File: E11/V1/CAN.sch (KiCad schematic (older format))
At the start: 21 parts, among them J401 649006227222, J402 649006227222, U401 SN65HVD232DR

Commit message: update for missing resistor
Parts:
- removed J401, J402: 649006227222, Connectors:649006227222, symbol Connectors:649006227222
- added J401, J402: 64900621122, Connectors:64900621122, symbol Connectors:64900621122
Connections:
- wire segments 67 -> 87
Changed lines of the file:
@@
 EESchema Schematic File Version 4
+LIBS:Slave-cache
 EELAYER 30 0
 EELAYER END
@@
 	2900 3800 3100 3800
 Wire Wire Line
-	1700 4000 3100 4000
+	1700 4000 1800 4000
 Connection ~ 1800 4000
 Wire Wire Line
@@
 	2900 3400 2800 3400
 Wire Wire Line
-	2900 2900 2900 3800
+	2900 2900 2900 3000
 Connection ~ 2900 3400
 $Comp
@@
 	2500 3000 2400 3000
 Wire Wire Line
-	2400 3000 2400 3500
+	2400 3000 2400 3400
 Connection ~ 2400 3400
 $Comp
@@
 	6300 3200 6300 3300
 Wire Wire Line
-	5300 5100 6400 5100
-Wire Wire Line
-	5400 4900 6400 4900
+	5300 5100 5600 5100
+Wire Wire Line
+	5400 4900 6000 4900
 Wire Wire Line
 	5400 4000 5400 4900
 Wire Wire Line
-	3800 4000 5400 4000
-Wire Wire Line
-	3800 4200 5300 4200
+	3800 4000 4200 4000
+Wire Wire Line
+	3800 4200 4200 4200
 Wire Wire Line
 	5300 4200 5300 5100
 Wire Wire Line
-	5100 2500 6500 2500
+	5100 2500 5700 2500
 Wire Wire Line
 	5700 2500 5700 2900
 Wire Wire Line
-	5200 2700 6500 2700
+	5200 2700 6200 2700
 Wire Wire Line
 	6300 2700 6300 2900
@@
 Connection ~ 6200 2700
 $Comp
-L Connectors:649006227222 J401
-U 1 1 593E0605
-P 7100 1900
-F 0 "J401" H 7100 2200 60  0000 C CNN
-F 1 "649006227222" H 7100 1750 60  0000 C CNN
-F 2 "Connectors:649006227222" H 7100 1000 60  0001 C CNN
-F 3 "http://katalog.we-online.de/em/datasheet/649006227222.pdf" H 7100 900 60  0001 C CNN
-F 4 "Digikey" H 7100 1500 60  0001 C CNN "Supplier"
-F 5 "732-1939-ND" H 7100 1400 60  0001 C CNN "Supplier Part Number"
-F 6 "Wurth Electronics Inc." H 7100 1300 60  0001 C CNN "Manufacturer"
-F 7 "649006227222" H 7100 1200 60  0001 C CNN "Manufacturer Part Number"
-F 8 "HEADER MALE DUAL ANGLE W/MNT 6P" H 7100 1100 60  0001 C CNN "Description"
-	1    7100 1900
-	1    0    0    -1
-$EndComp
-$Comp
 L Resistors:RC0805JR-070RL R403
 U 1 1 593E067F
@@
 Text Label 6500 4300 0    60   ~ 0
 CAN_N
-$Comp
-L Connectors:649006227222 J402
-U 1 1 593E12E2
-P 7100 4300
-F 0 "J402" H 7100 4600 60  0000 C CNN
-F 1 "649006227222" H 7100 4150 60  0000 C CNN
-F 2 "Connectors:649006227222" H 7100 3400 60  0001 C CNN
-F 3 "http://katalog.we-online.de/em/datasheet/649006227222.pdf" H 7100 3300 60  0001 C CNN
-F 4 "Digikey" H 7100 3900 60  0001 C CNN "Supplier"
-F 5 "732-1939-ND" H 7100 3800 60  0001 C CNN "Supplier Part Number"
-F 6 "Wurth Electronics Inc." H 7100 3700 60  0001 C CNN "Manufacturer"
-F 7 "649006227222" H 7100 3600 60  0001 C CNN "Manufacturer Part Number"
-F 8 "HEADER MALE DUAL ANGLE W/MNT 6P" H 7100 3500 60  0001 C CNN "Description"
-	1    7100 4300
-	1    0    0    -1
-$EndComp
 $Comp
 L Resistors:RC0805JR-070RL R404
@@
 $EndComp
 Wire Wire Line
-	2300 4200 2600 4200
+	2300 4200 2500 4200
 Wire Wire Line
 	3000 4200 3100 4200
+Wire Wire Line
+	1800 4000 1900 4000
+Wire Wire Line
+	2900 3400 2900 3800
+Wire Wire Line
+	2900 3000 2900 3400
+Wire Wire Line
+	2400 3400 2400 3500
+Wire Wire Line
+	5200 4200 5300 4200
+Wire Wire Line
+	6300 2700 6500 2700
+Wire Wire Line
+	5700 2500 6300 2500
+Wire Wire Line
+	5100 4000 5400 4000
+Wire Wire Line
+	4400 4000 5100 4000
+Wire Wire Line
+	4800 4200 5200 4200
+Wire Wire Line
+	4200 4200 4800 4200
+Wire Wire Line
+	4200 4000 4400 4000
+Wire Wire Line
+	1900 4000 3100 4000
+Wire Wire Line
+	2500 4200 2600 4200
+Wire Wire Line
+	5600 5100 6100 5100
+Wire Wire Line
+	6100 5100 6400 5100
+Wire Wire Line
+	6200 4900 6400 4900
+Wire Wire Line
+	6300 2500 6500 2500
+Wire Wire Line
+	6200 2700 6300 2700
+Wire Wire Line
+	6000 4900 6200 4900
+$Comp
+L Connectors:64900621122 J401
+U 1 1 5EB2172E
+P 7100 1900
+F 0 "J401" H 7100 2337 60  0000 C CNN
+F 1 "64900621122" H 7100 2231 60  0000 C CNN
+F 2 "Connectors:64900621122" H 7100 1000 60  0001 C CNN
+F 3 "http://katalog.we-online.de/em/datasheet/6490xx21122.pdf" H 7100 900 60  0001 C CNN
+F 4 "Digikey" H 7100 1500 60  0001 C CNN "Supplier"
+F 5 "732-1929-ND" H 7100 1400 60  0001 C CNN "Supplier Part Number"
+F 6 "Wurth Electronics Inc." H 7100 1300 60  0001 C CNN "Manufacturer"
+F 7 "64900621122" H 7100 1200 60  0001 C CNN "Manufacturer Part Number"
+F 8 "HEADER MALE 4.20MM DUAL VERT 6P" H 7100 1100 60  0001 C CNN "Description"
+	1    7100 1900
+	1    0    0    -1
+$EndComp
+$Comp
+L Connectors:64900621122 J402
+U 1 1 5EB22637
+P 7100 4300
+F 0 "J402" H 7100 4737 60  0000 C CNN
+F 1 "64900621122" H 7100 4631 60  0000 C CNN
+F 2 "Connectors:64900621122" H 7100 3400 60  0001 C CNN
+F 3 "http://katalog.we-online.de/em/datasheet/6490xx21122.pdf" H 7100 3300 60  0001 C CNN
+F 4 "Digikey" H 7100 3900 60  0001 C CNN "Supplier"
+F 5 "732-1929-ND" H 7100 3800 60  0001 C CNN "Supplier Part Number"
+F 6 "Wurth Electronics Inc." H 7100 3700 60  0001 C CNN "Manufacturer"
+F 7 "64900621122" H 7100 3600 60  0001 C CNN "Manufacturer Part Number"
+F 8 "HEADER MALE 4.20MM DUAL VERT 6P" H 7100 3500 60  0001 C CNN "Description"
+	1    7100 4300
+	1    0    0    -1
+$EndComp
 $EndSCHEMATC

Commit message: most of the parts have been migrated to new board outline
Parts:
- C401: footprint Capacitors:C0805 -> Capacitors:C0603; symbol Capacitors:885012107015 -> Capacitors:885012106022; Description CAP CER 1UF 25V X5R 0805 -> CAP CER 1UF 25V X5R 0603; Manufacturer Part Number 885012107015 -> 885012106022; Supplier Part Number 732-7625-1-ND -> 732-7919-2-ND
- C402, C403, C406, C407: footprint Capacitors:C0805 -> Capacitors:C0603; symbol Capacitors:885012007053 -> Capacitors:885012006053; Description CAP CER 22PF 50V C0G/NP0 0805 -> CAP CER 22PF 50V X7R 0603; Manufacturer Part Number 885012007053 -> 885012206077; Supplier Part Number 732-7848-1-ND -> 732-7995-2-ND
- C404: footprint Capacitors:C0805 -> Capacitors:C0603; symbol Capacitors:885012207098 -> Capacitors:885012206095; Description CAP CER 0.1UF 50V X7R 0805 -> CAP CER 0.1UF 50V X7R 0603; Manufacturer Part Number 885012207098 -> 885012206095; Supplier Part Number 732-8080-1-ND -> 732-8013-2-ND
- C405: footprint Capacitors:C0805 -> Capacitors:C0603; symbol Capacitors:885012207080 -> Capacitors:885012206077; Description CAP CER 100PF 50V X7R 0805 -> CAP CER 100PF 50V X7R 0603; Manufacturer Part Number 885012207080 -> 885012206077; Supplier Part Number 732-8062-1-ND -> 732-7995-2-ND
- R401, R405: footprint Resistors:R0805 -> Resistors:R0603; symbol Resistors:RC0805JR-07100RL -> Resistors:RNCP0603FTD100R; Description RES SMD 100 OHM 5% 1/8W 0805 -> RES 100 OHM 1% 1/8W 0603; Manufacturer Yageo -> Stackpole Electronics Inc; Manufacturer Part Number RC0805JR-07100RL -> RNCP0603FTD100R; Supplier Part Number 311-100ARCT-ND -> RNCP0603FTD100RTR-ND
- R403, R404: footprint Resistors:R0805 -> Resistors:R0603; symbol Resistors:RC0805JR-070RL -> Resistors:RC0603JR-070RL; Description RES SMD 0.0 OHM JUMPER 1/8W 0805 -> RES SMD 0 OHM JUMPER 1/10W 0603; Manufacturer Part Number RC0805JR-070RL -> RC0603JR-070RL; Puissance (Watts) 1/8W -> 1/10W; Supplier Part Number 311-0.0ARCT-ND -> 311-0.0GRTR-ND; Tolerance (%) 0 -> Jumper

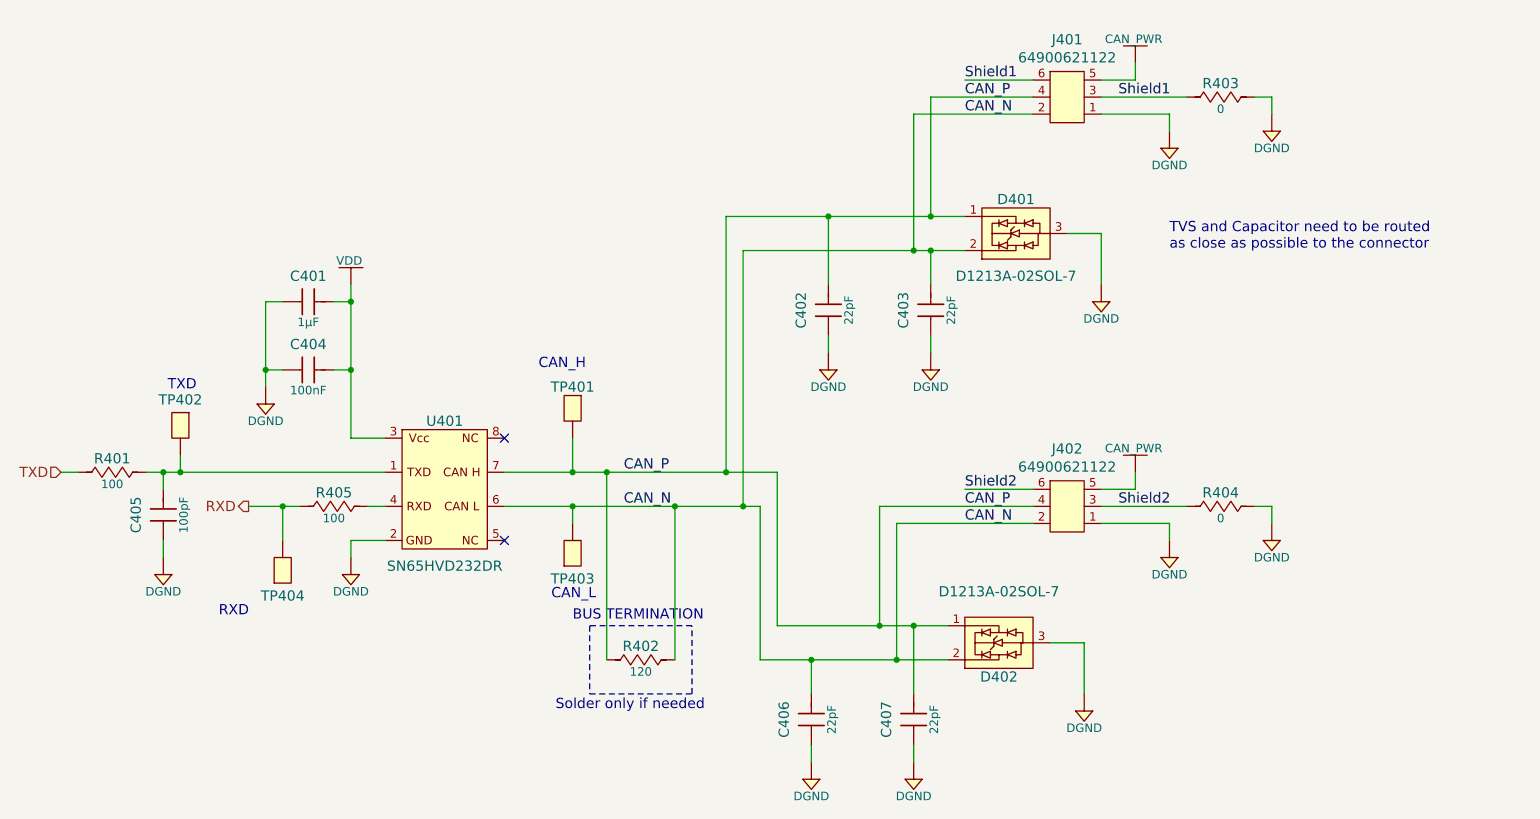
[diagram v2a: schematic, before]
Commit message: initial component placement done
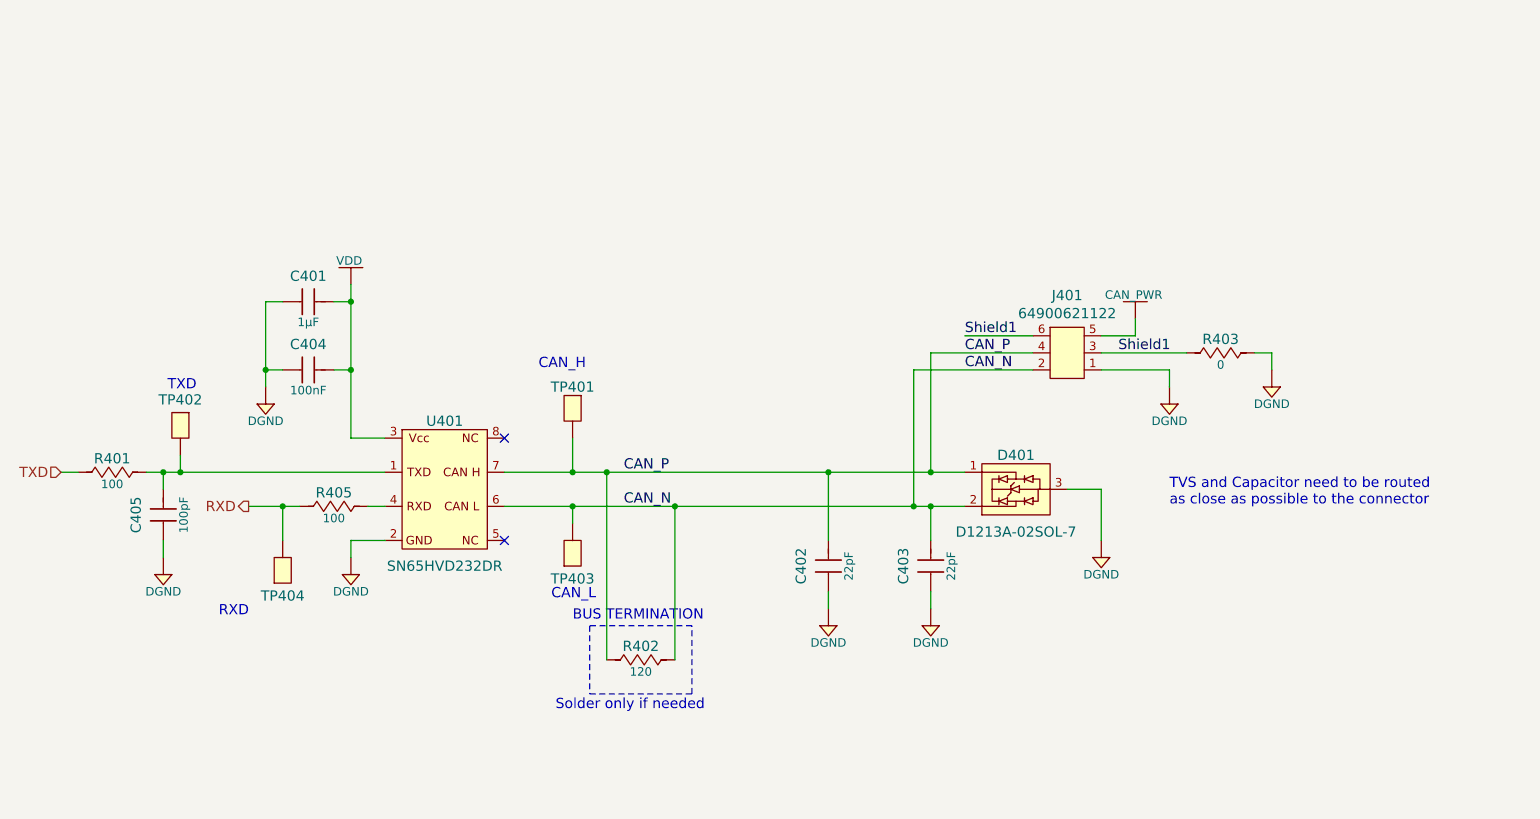
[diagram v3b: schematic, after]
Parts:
- removed C406, C407: 885012007053, Capacitors:C0603, symbol Capacitors:885012006053
- removed D402: D1213A-02SOL-7, IC:SOT-23-3, symbol Diodes:D1213A-02SOL-7
- removed J402: 64900621122, Connectors:64900621122, symbol Connectors:64900621122
- removed R404: RC0805JR-070RL, Resistors:R0603, symbol Resistors:RC0603JR-070RL
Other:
- moved on the sheet: C402, C403, D401, J401, R403
